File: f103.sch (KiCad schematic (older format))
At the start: 211 parts, among them J1 Conn_01x04_Female, J2 Conn_01x01_Male, J3 Conn_01x01_Male, J4 Conn_01x01_Male, Q1 2N7002, SW1 Rotary_Encoder_Switch, U1 STM32F103CBTx, U2 XC6206P332MR, U3 SRV05-4, Y1 8MHz

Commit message: DRC I
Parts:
- removed J1: Conn_01x04_Female, Connector_PinHeader_2.54mm:PinHeader_1x04_P2.54mm_Vertical, symbol Connector:Conn_01x04_Female
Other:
- note removed: "USB Breakout"
- moved on the sheet: C10, C11, U2, U3
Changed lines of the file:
@@
 EESchema Schematic File Version 4
+LIBS:f103-cache
 EELAYER 30 0
 EELAYER END
@@
 	1    0    0    -1
 $EndComp
-Text GLabel 5800 8050 2    50   Input ~ 0
+Text GLabel 4800 8050 2    50   Input ~ 0
 D-
 $Comp
 L power:+5V #PWR0116
 U 1 1 5FF47CBA
-P 5300 7650
-F 0 "#PWR0116" H 5300 7500 50  0001 C CNN
-F 1 "+5V" H 5315 7823 50  0000 C CNN
-F 2 "" H 5300 7650 50  0001 C CNN
-F 3 "" H 5300 7650 50  0001 C CNN
-	1    5300 7650
+P 4300 7650
+F 0 "#PWR0116" H 4300 7500 50  0001 C CNN
+F 1 "+5V" H 4315 7823 50  0000 C CNN
+F 2 "" H 4300 7650 50  0001 C CNN
+F 3 "" H 4300 7650 50  0001 C CNN
+	1    4300 7650
 	1    0    0    -1
 $EndComp
@@
 L power:GND #PWR0115
 U 1 1 5FF463F5
-P 5300 8650
-F 0 "#PWR0115" H 5300 8400 50  0001 C CNN
-F 1 "GND" H 5305 8477 50  0000 C CNN
-F 2 "" H 5300 8650 50  0001 C CNN
-F 3 "" H 5300 8650 50  0001 C CNN
-	1    5300 8650
+P 4300 8650
+F 0 "#PWR0115" H 4300 8400 50  0001 C CNN
+F 1 "GND" H 4305 8477 50  0000 C CNN
+F 2 "" H 4300 8650 50  0001 C CNN
+F 3 "" H 4300 8650 50  0001 C CNN
+	1    4300 8650
 	1    0    0    -1
 $EndComp
-Text GLabel 5800 8250 2    50   Input ~ 0
+Text GLabel 4800 8250 2    50   Input ~ 0
 D+
 $Comp
 L Power_Protection:SRV05-4 U3
 U 1 1 5FF42D8B
-P 5300 8150
-F 0 "U3" H 5000 8800 50  0000 C CNN
-F 1 "SRV05-4" H 5000 8700 50  0000 C CNN
-F 2 "Package_TO_SOT_SMD:SOT-23-6" H 6000 7700 50  0001 C CNN
-F 3 "http://www.onsemi.com/pub/Collateral/SRV05-4-D.PDF" H 5300 8150 50  0001 C CNN
-F 4 "C85364" H 5300 8150 50  0001 C CNN "Part #"
-	1    5300 8150
+P 4300 8150
+F 0 "U3" H 4000 8800 50  0000 C CNN
+F 1 "SRV05-4" H 4000 8700 50  0000 C CNN
+F 2 "Package_TO_SOT_SMD:SOT-23-6" H 5000 7700 50  0001 C CNN
+F 3 "http://www.onsemi.com/pub/Collateral/SRV05-4-D.PDF" H 4300 8150 50  0001 C CNN
+F 4 "C85364" H 4300 8150 50  0001 C CNN "Part #"
+	1    4300 8150
 	1    0    0    -1
 $EndComp
 Wire Wire Line
-	7450 8550 7000 8550
-Connection ~ 7000 8550
+	6950 8550 6500 8550
+Connection ~ 6500 8550
 Wire Wire Line
-	6550 8550 7000 8550
-Connection ~ 6550 8250
+	6050 8550 6500 8550
+Connection ~ 6050 8250
 Wire Wire Line
-	6550 8250 6450 8250
+	6050 8250 5950 8250
 Wire Wire Line
-	6550 8250 6550 8350
+	6050 8250 6050 8350
 Wire Wire Line
-	6700 8250 6550 8250
-Connection ~ 7450 8250
+	6200 8250 6050 8250
+Connection ~ 6950 8250
 Wire Wire Line
-	7450 8250 7550 8250
+	6950 8250 7050 8250
 Wire Wire Line
-	7450 8250 7450 8350
+	6950 8250 6950 8350
 Wire Wire Line
-	7300 8250 7450 8250
+	6800 8250 6950 8250
 $Comp
 L Device:C_Small C11
 U 1 1 5FF82A05
-P 7450 8450
-F 0 "C11" H 7542 8496 50  0000 L CNN
-F 1 "1uF" H 7542 8405 50  0000 L CNN
-F 2 "Capacitor_SMD:C_0603_1608Metric" H 7450 8450 50  0001 C CNN
-F 3 "~" H 7450 8450 50  0001 C CNN
-	1    7450 8450
+P 6950 8450
+F 0 "C11" H 7042 8496 50  0000 L CNN
+F 1 "1uF" H 7042 8405 50  0000 L CNN
+F 2 "Capacitor_SMD:C_0603_1608Metric" H 6950 8450 50  0001 C CNN
+F 3 "~" H 6950 8450 50  0001 C CNN
+	1    6950 8450
 	1    0    0    -1
 $EndComp
@@
 L Device:C_Small C10
 U 1 1 5FF81242
-P 6550 8450
-F 0 "C10" H 6642 8496 50  0000 L CNN
-F 1 "1uF" H 6642 8405 50  0000 L CNN
-F 2 "Capacitor_SMD:C_0603_1608Metric" H 6550 8450 50  0001 C CNN
-F 3 "~" H 6550 8450 50  0001 C CNN
-	1    6550 8450
+P 6050 8450
+F 0 "C10" H 6142 8496 50  0000 L CNN
+F 1 "1uF" H 6142 8405 50  0000 L CNN
+F 2 "Capacitor_SMD:C_0603_1608Metric" H 6050 8450 50  0001 C CNN
+F 3 "~" H 6050 8450 50  0001 C CNN
+	1    6050 8450
 	1    0    0    -1
 $EndComp
@@
 L power:GND #PWR0119
 U 1 1 5FF7FCD1
-P 7000 8550
-F 0 "#PWR0119" H 7000 8300 50  0001 C CNN
-F 1 "GND" H 7005 8377 50  0000 C CNN
-F 2 "" H 7000 8550 50  0001 C CNN
-F 3 "" H 7000 8550 50  0001 C CNN
-	1    7000 8550
+P 6500 8550
+F 0 "#PWR0119" H 6500 8300 50  0001 C CNN
+F 1 "GND" H 6505 8377 50  0000 C CNN
+F 2 "" H 6500 8550 50  0001 C CNN
+F 3 "" H 6500 8550 50  0001 C CNN
+	1    6500 8550
 	1    0    0    -1
 $EndComp
@@
 L power:+3.3V #PWR0118
 U 1 1 5FF7E7EA
-P 7550 8250
-F 0 "#PWR0118" H 7550 8100 50  0001 C CNN
-F 1 "+3.3V" H 7565 8423 50  0000 C CNN
-F 2 "" H 7550 8250 50  0001 C CNN
-F 3 "" H 7550 8250 50  0001 C CNN
-	1    7550 8250
+P 7050 8250
+F 0 "#PWR0118" H 7050 8100 50  0001 C CNN
+F 1 "+3.3V" H 7065 8423 50  0000 C CNN
+F 2 "" H 7050 8250 50  0001 C CNN
+F 3 "" H 7050 8250 50  0001 C CNN
+	1    7050 8250
 	1    0    0    -1
 $EndComp
@@
 L power:+5V #PWR0117
 U 1 1 5FF7D017
-P 6450 8250
-F 0 "#PWR0117" H 6450 8100 50  0001 C CNN
-F 1 "+5V" H 6465 8423 50  0000 C CNN
-F 2 "" H 6450 8250 50  0001 C CNN
-F 3 "" H 6450 8250 50  0001 C CNN
-	1    6450 8250
+P 5950 8250
+F 0 "#PWR0117" H 5950 8100 50  0001 C CNN
+F 1 "+5V" H 5965 8423 50  0000 C CNN
+F 2 "" H 5950 8250 50  0001 C CNN
+F 3 "" H 5950 8250 50  0001 C CNN
+	1    5950 8250
 	1    0    0    -1
 $EndComp
@@
 L Regulator_Linear:MCP1700-3302E_SOT23 U2
 U 1 1 5FF7B9AE
-P 7000 8250
-F 0 "U2" H 7000 8492 50  0000 C CNN
-F 1 "XC6206P332MR" H 7000 8401 50  0000 C CNN
-F 2 "Package_TO_SOT_SMD:SOT-23" H 7000 8475 50  0001 C CNN
-F 3 "http://ww1.microchip.com/downloads/en/DeviceDoc/20001826D.pdf" H 7000 8250 50  0001 C CNN
-F 4 "C5446" H 7000 8250 50  0001 C CNN "Part #"
-	1    7000 8250
+P 6500 8250
+F 0 "U2" H 6500 8492 50  0000 C CNN
+F 1 "XC6206P332MR" H 6500 8401 50  0000 C CNN
+F 2 "Package_TO_SOT_SMD:SOT-23" H 6500 8475 50  0001 C CNN
+F 3 "http://ww1.microchip.com/downloads/en/DeviceDoc/20001826D.pdf" H 6500 8250 50  0001 C CNN
+F 4 "C5446" H 6500 8250 50  0001 C CNN "Part #"
+	1    6500 8250
 	1    0    0    -1
 $EndComp
@@
 Text Notes 1950 7300 0    98   ~ 20
 USB
-Text Notes 6500 7300 0    98   ~ 20
+Text Notes 6000 7300 0    98   ~ 20
 Voltage Reg.
-Text Notes 5150 7300 0    98   ~ 20
+Text Notes 4150 7300 0    98   ~ 20
 ESD
 NoConn ~ 2050 8400
@@
 	1950 3900 2200 3900
 Connection ~ 2200 3900
-$Comp
-L power:VBUS #PWR0131
-U 1 1 60058240
-P 3500 7900
-F 0 "#PWR0131" H 3500 7750 50  0001 C CNN
-F 1 "VBUS" H 3515 8073 50  0000 C CNN
-F 2 "" H 3500 7900 50  0001 C CNN
-F 3 "" H 3500 7900 50  0001 C CNN
-	1    3500 7900
-	1    0    0    -1
-$EndComp
-$Comp
-L power:GND #PWR0132
-U 1 1 60057E3C
-P 3500 8200
-F 0 "#PWR0132" H 3500 7950 50  0001 C CNN
-F 1 "GND" H 3505 8027 50  0000 C CNN
-F 2 "" H 3500 8200 50  0001 C CNN
-F 3 "" H 3500 8200 50  0001 C CNN
-	1    3500 8200
-	1    0    0    -1
-$EndComp
-Text GLabel 3500 8100 0    50   Input ~ 0
-D+
-Text GLabel 3500 8000 0    50   Input ~ 0
-D-
-$Comp
-L Connector:Conn_01x04_Female J1
-U 1 1 60056004
-P 3700 8000
-F 0 "J1" H 3728 7976 50  0000 L CNN
-F 1 "Conn_01x04_Female" H 3728 7885 50  0000 L CNN
-F 2 "Connector_PinHeader_2.54mm:PinHeader_1x04_P2.54mm_Vertical" H 3700 8000 50  0001 C CNN
-F 3 "~" H 3700 8000 50  0001 C CNN
-	1    3700 8000
-	1    0    0    -1
-$EndComp
 Wire Notes Line
 	550  8900 7800 8900
-Text Notes 3400 7300 0    98   ~ 20
-USB Breakout
 $Comp
 L Device:Rotary_Encoder_Switch SW1

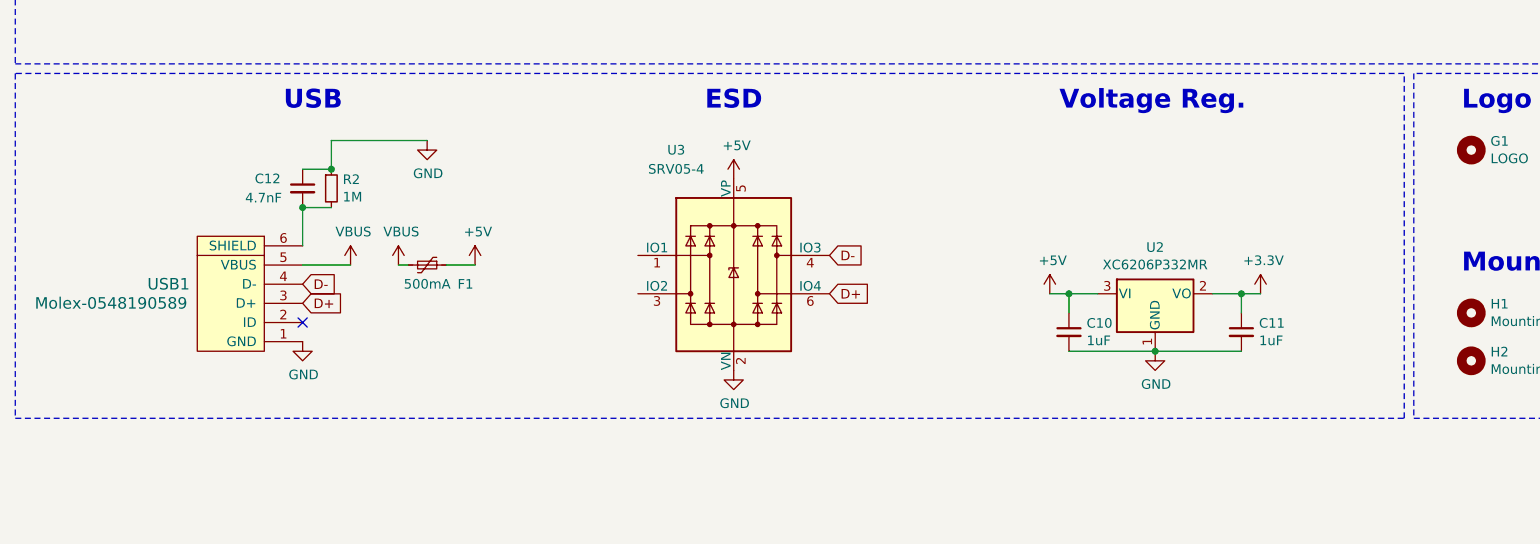
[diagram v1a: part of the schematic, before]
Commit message: DRC III
Switch to usb type-C
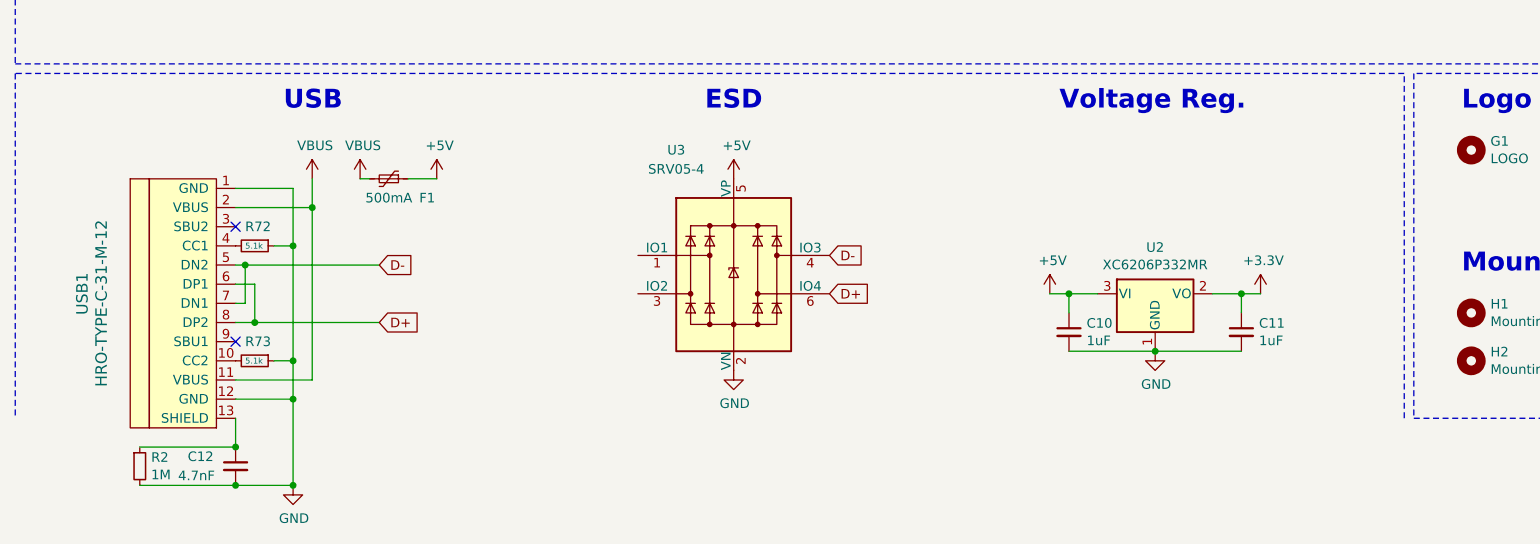
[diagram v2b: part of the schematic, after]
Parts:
- removed USB1: Molex-0548190589, MINI:Molex-0548190589, symbol RKP:Molex-0548190589
- added R72, R73: 5.1k, Resistor_SMD:R_0603_1608Metric, symbol Device:R_Small
- added USB1: HRO-TYPE-C-31-M-12, Type C:HRO-TYPE-C-31-M-12-jlc, symbol Type-C:HRO-TYPE-C-31-M-12
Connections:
- net D+: now also USB1.6 (DP1), USB1.8 (DP2)
- net D-: now also USB1.5 (DN2), USB1.7 (DN1)
- net GND: now also C12.2, R2.2, R72.1, R73.1, USB1.1 (GND), USB1.12 (GND); no longer C12.1, R2.1
- net VBUS: now also USB1.11 (VBUS), USB1.2 (VBUS)
- new net: C12.1, R2.1, USB1.13 (SHIELD)
- new net: R73.2, USB1.10 (CC2)
- new net: R72.2, USB1.4 (CC1)
- no-connect marks 9 -> 10
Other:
- moved on the sheet: C12, F1, R2
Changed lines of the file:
@@
 $EndComp
 Wire Wire Line
-	2950 8100 2800 8100
-$Comp
-L RKP:Molex-0548190589 USB1
-U 1 1 5FEC9337
-P 1750 8300
-F 0 "USB1" V 1850 8700 60  0000 C CNN
-F 1 "Molex-0548190589" V 1750 9000 60  0000 C CNN
-F 2 "MINI:Molex-0548190589" H 1750 8300 60  0001 C CNN
-F 3 "" H 1750 8300 60  0001 C CNN
-	1    1750 8300
-	0    -1   -1   0
-$EndComp
+	2750 7650 2600 7650
 $Comp
 L Device:R_Small R1
@@
 $EndComp
 $Comp
-L power:GND #PWR0125
-U 1 1 600ED86F
-P 2700 7450
-F 0 "#PWR0125" H 2700 7200 50  0001 C CNN
-F 1 "GND" H 2705 7277 50  0000 C CNN
-F 2 "" H 2700 7450 50  0001 C CNN
-F 3 "" H 2700 7450 50  0001 C CNN
-	1    2700 7450
-	1    0    0    -1
-$EndComp
-$Comp
 L Device:R_Small R2
 U 1 1 600E6AC0
-P 2200 7700
-F 0 "R2" H 2259 7746 50  0000 L CNN
-F 1 "1M" H 2259 7655 50  0000 L CNN
-F 2 "Resistor_SMD:R_0603_1608Metric" H 2200 7700 50  0001 C CNN
-F 3 "~" H 2200 7700 50  0001 C CNN
-	1    2200 7700
+P 1200 9150
+F 0 "R2" H 1259 9196 50  0000 L CNN
+F 1 "1M" H 1259 9105 50  0000 L CNN
+F 2 "Resistor_SMD:R_0603_1608Metric" H 1200 9150 50  0001 C CNN
+F 3 "~" H 1200 9150 50  0001 C CNN
+	1    1200 9150
 	1    0    0    -1
 $EndComp
@@
 L Device:C_Small C12
 U 1 1 600E54EB
-P 2050 7700
-F 0 "C12" H 1800 7750 50  0000 L CNN
-F 1 "4.7nF" H 1750 7650 50  0000 L CNN
-F 2 "Capacitor_SMD:C_0603_1608Metric" H 2050 7700 50  0001 C CNN
-F 3 "~" H 2050 7700 50  0001 C CNN
-	1    2050 7700
+P 1700 9150
+F 0 "C12" H 1450 9200 50  0000 L CNN
+F 1 "4.7nF" H 1400 9100 50  0000 L CNN
+F 2 "Capacitor_SMD:C_0603_1608Metric" H 1700 9150 50  0001 C CNN
+F 3 "~" H 1700 9150 50  0001 C CNN
+	1    1700 9150
 	1    0    0    -1
 $EndComp
@@
 L power:+5V #PWR0123
 U 1 1 5FFD8345
-P 2950 8100
-F 0 "#PWR0123" H 2950 7950 50  0001 C CNN
-F 1 "+5V" H 2965 8273 50  0000 C CNN
-F 2 "" H 2950 8100 50  0001 C CNN
-F 3 "" H 2950 8100 50  0001 C CNN
-	1    2950 8100
+P 2750 7650
+F 0 "#PWR0123" H 2750 7500 50  0001 C CNN
+F 1 "+5V" H 2765 7823 50  0000 C CNN
+F 2 "" H 2750 7650 50  0001 C CNN
+F 3 "" H 2750 7650 50  0001 C CNN
+	1    2750 7650
 	1    0    0    -1
 $EndComp
@@
 L Device:Polyfuse_Small F1
 U 1 1 5FFD669E
-P 2700 8100
-F 0 "F1" V 2800 8300 50  0000 C CNN
-F 1 "500mA" V 2800 8100 50  0000 C CNN
-F 2 "Fuse:Fuse_1206_3216Metric" H 2750 7900 50  0001 L CNN
-F 3 "~" H 2700 8100 50  0001 C CNN
-F 4 "C369159" V 2700 8100 50  0001 C CNN "Part #"
-	1    2700 8100
+P 2500 7650
+F 0 "F1" V 2600 7850 50  0000 C CNN
+F 1 "500mA" V 2600 7650 50  0000 C CNN
+F 2 "Fuse:Fuse_1206_3216Metric" H 2550 7450 50  0001 L CNN
+F 3 "~" H 2500 7650 50  0001 C CNN
+F 4 "C369159" V 2500 7650 50  0001 C CNN "Part #"
+	1    2500 7650
 	0    1    1    0
 $EndComp
@@
 L power:GND #PWR0120
 U 1 1 5FFD3143
-P 2050 8500
-F 0 "#PWR0120" H 2050 8250 50  0001 C CNN
-F 1 "GND" H 2055 8327 50  0000 C CNN
-F 2 "" H 2050 8500 50  0001 C CNN
-F 3 "" H 2050 8500 50  0001 C CNN
-	1    2050 8500
-	1    0    0    -1
-$EndComp
-Text GLabel 2050 8300 2    50   Input ~ 0
-D+
-Text GLabel 2050 8200 2    50   Input ~ 0
-D-
+P 2000 9250
+F 0 "#PWR0120" H 2000 9000 50  0001 C CNN
+F 1 "GND" H 2005 9077 50  0000 C CNN
+F 2 "" H 2000 9250 50  0001 C CNN
+F 3 "" H 2000 9250 50  0001 C CNN
+	1    2000 9250
+	1    0    0    -1
+$EndComp
 Text GLabel 13500 6500 2    50   Input ~ 0
 BOOT0
@@
 $EndComp
 Wire Wire Line
-	2300 8100 2050 8100
-Wire Wire Line
-	2550 8100 2600 8100
-Wire Wire Line
-	2050 8000 2050 7800
-Wire Wire Line
-	2050 7800 2200 7800
-Connection ~ 2050 7800
-Wire Wire Line
-	2050 7600 2200 7600
-Wire Wire Line
-	2200 7600 2200 7450
-Wire Wire Line
-	2200 7450 2700 7450
-Connection ~ 2200 7600
-$Comp
-L power:VBUS #PWR0129
-U 1 1 6015B2FA
-P 2300 8100
-F 0 "#PWR0129" H 2300 7950 50  0001 C CNN
-F 1 "VBUS" H 2315 8273 50  0000 C CNN
-F 2 "" H 2300 8100 50  0001 C CNN
-F 3 "" H 2300 8100 50  0001 C CNN
-	1    2300 8100
-	1    0    0    -1
-$EndComp
+	2350 7650 2400 7650
 $Comp
 L power:VBUS #PWR0130
 U 1 1 6015CEDE
-P 2550 8100
-F 0 "#PWR0130" H 2550 7950 50  0001 C CNN
-F 1 "VBUS" H 2565 8273 50  0000 C CNN
-F 2 "" H 2550 8100 50  0001 C CNN
-F 3 "" H 2550 8100 50  0001 C CNN
-	1    2550 8100
+P 2350 7650
+F 0 "#PWR0130" H 2350 7500 50  0001 C CNN
+F 1 "VBUS" H 2365 7823 50  0000 C CNN
+F 2 "" H 2350 7650 50  0001 C CNN
+F 3 "" H 2350 7650 50  0001 C CNN
+	1    2350 7650
 	1    0    0    -1
 $EndComp
@@
 Text Notes 4150 7300 0    98   ~ 20
 ESD
-NoConn ~ 2050 8400
 NoConn ~ 14000 3400
 NoConn ~ 14000 3500
@@
 	1950 3900 2200 3900
 Connection ~ 2200 3900
-Wire Notes Line
-	550  8900 7800 8900
 $Comp
 L Device:Rotary_Encoder_Switch SW1
@@
 	10700 1800 10700 2700
 Connection ~ 10600 1900
+$Comp
+L Type-C:HRO-TYPE-C-31-M-12 USB1
+U 1 1 601D2A97
+P 1600 8250
+F 0 "USB1" V 900 8250 60  0000 C CNN
+F 1 "HRO-TYPE-C-31-M-12" V 1000 8200 60  0000 C CNN
+F 2 "Type C:HRO-TYPE-C-31-M-12-jlc" H 1600 8250 60  0001 C CNN
+F 3 "" H 1600 8250 60  0001 C CNN
+	1    1600 8250
+	1    0    0    -1
+$EndComp
+Wire Wire Line
+	1200 9050 1700 9050
+Wire Wire Line
+	1700 9050 1700 8900
+Connection ~ 1700 9050
+Wire Wire Line
+	1200 9250 1700 9250
+$Comp
+L Device:R_Small R73
+U 1 1 6023F787
+P 1800 8600
+F 0 "R73" V 1700 8550 50  0000 L CNN
+F 1 "5.1k" V 1800 8550 31  0000 L CNN
+F 2 "Resistor_SMD:R_0603_1608Metric" H 1800 8600 50  0001 C CNN
+F 3 "~" H 1800 8600 50  0001 C CNN
+	1    1800 8600
+	0    1    1    0
+$EndComp
+$Comp
+L Device:R_Small R72
+U 1 1 60241B9D
+P 1800 8000
+F 0 "R72" V 1700 7950 50  0000 L CNN
+F 1 "5.1k" V 1800 7950 31  0000 L CNN
+F 2 "Resistor_SMD:R_0603_1608Metric" H 1800 8000 50  0001 C CNN
+F 3 "~" H 1800 8000 50  0001 C CNN
+	1    1800 8000
+	0    1    1    0
+$EndComp
+Wire Wire Line
+	1700 7700 2000 7700
+Wire Wire Line
+	2000 7700 2000 8000
+Wire Wire Line
+	2000 8800 1700 8800
+Wire Wire Line
+	1900 8600 2000 8600
+Connection ~ 2000 8600
+Wire Wire Line
+	2000 8600 2000 8800
+Wire Wire Line
+	1900 8000 2000 8000
+Connection ~ 2000 8000
+Wire Wire Line
+	2000 8000 2000 8600
+Wire Wire Line
+	1700 8100 1750 8100
+Wire Wire Line
+	1750 8100 1750 8300
+Wire Wire Line
+	1750 8300 1700 8300
+Wire Wire Line
+	1750 8100 2450 8100
+Connection ~ 1750 8100
+Text GLabel 2450 8100 2    50   Input ~ 0
+D-
+Wire Wire Line
+	1700 8200 1800 8200
+Wire Wire Line
+	1800 8200 1800 8400
+Wire Wire Line
+	1800 8400 1700 8400
+Wire Wire Line
+	1800 8400 2450 8400
+Connection ~ 1800 8400
+Text GLabel 2450 8400 2    50   Input ~ 0
+D+
+Wire Wire Line
+	1700 7800 2100 7800
+Wire Wire Line
+	2100 7800 2100 8700
+Wire Wire Line
+	2100 8700 1700 8700
+$Comp
+L power:VBUS #PWR0125
+U 1 1 603FD33D
+P 2100 7650
+F 0 "#PWR0125" H 2100 7500 50  0001 C CNN
+F 1 "VBUS" H 2115 7823 50  0000 C CNN
+F 2 "" H 2100 7650 50  0001 C CNN
+F 3 "" H 2100 7650 50  0001 C CNN
+	1    2100 7650
+	1    0    0    -1
+$EndComp
+Wire Wire Line
+	2100 7650 2100 7800
+Connection ~ 2100 7800
+NoConn ~ 1700 7900
+NoConn ~ 1700 8500
+Wire Wire Line
+	2000 8800 2000 9250
+Wire Wire Line
+	2000 9250 1700 9250
+Connection ~ 2000 8800
+Connection ~ 1700 9250
+Connection ~ 2000 9250
 $EndSCHEMATC

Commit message: DRC IV
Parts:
- USB1: footprint Type C:HRO-TYPE-C-31-M-12-jlc -> edits:HRO-TYPE-C-31-M-12-jlc
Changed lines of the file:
@@
 F 0 "USB1" V 900 8250 60  0000 C CNN
 F 1 "HRO-TYPE-C-31-M-12" V 1000 8200 60  0000 C CNN
-F 2 "Type C:HRO-TYPE-C-31-M-12-jlc" H 1600 8250 60  0001 C CNN
+F 2 "edits:HRO-TYPE-C-31-M-12-jlc" H 1600 8250 60  0001 C CNN
 F 3 "" H 1600 8250 60  0001 C CNN
 	1    1600 8250

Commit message: Checking Datasheet
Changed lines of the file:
@@
 L power:GND #PWR0133
 U 1 1 600CA7BC
-P 950 2100
-F 0 "#PWR0133" H 950 1850 50  0001 C CNN
-F 1 "GND" H 955 1927 50  0000 C CNN
-F 2 "" H 950 2100 50  0001 C CNN
-F 3 "" H 950 2100 50  0001 C CNN
-	1    950  2100
+P 950 2350
+F 0 "#PWR0133" H 950 2100 50  0001 C CNN
+F 1 "GND" H 955 2177 50  0000 C CNN
+F 2 "" H 950 2350 50  0001 C CNN
+F 3 "" H 950 2350 50  0001 C CNN
+	1    950  2350
 	1    0    0    -1
 $EndComp
@@
 Connection ~ 1700 9250
 Connection ~ 2000 9250
+Wire Wire Line
+	950  2350 950  2100
 $EndSCHEMATC

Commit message: DRC Pass
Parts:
- removed J2, J3, J4: Conn_01x01_Male, TestPoint:TestPoint_Pad_D1.5mm, symbol Connector:Conn_01x01_Male
- added J1, J2, J3, J4: Conn_01x01_Female, TestPoint:TestPoint_Pad_D1.5mm, symbol Connector:Conn_01x01_Female
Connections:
- net +3V3: now also J4.1 (Pin_1)
- net C0: now also U1.20 (PB2); no longer U1.19 (PB1)
- net C1: now also U1.19 (PB1); no longer U1.18 (PB0)
- net C14: now also U1.3 (PC14); no longer U1.11 (PA1)
- net C2: now also U1.18 (PB0); no longer U1.17 (PA7)
- net C3: now also U1.17 (PA7); no longer U1.16 (PA6)
- net C4: now also U1.16 (PA6); no longer U1.15 (PA5)
- net C5: now also U1.15 (PA5); no longer U1.14 (PA4)
- net C6: now also U1.14 (PA4); no longer U1.13 (PA3)
- net C7: now also U1.22 (PB11); no longer U1.12 (PA2)
- net ENCA: now also U1.29 (PA8); no longer U1.30 (PA9)
- net ENCB: now also U1.30 (PA9); no longer U1.31 (PA10)
- net GND: now also J2.1 (Pin_1)
- net R0: now also U1.31 (PA10); no longer U1.29 (PA8)
- net R1: now also U1.21 (PB10); no longer U1.20 (PB2)
- net R3: now also U1.13 (PA3); no longer U1.21 (PB10)
- net R4: now also U1.12 (PA2); no longer U1.22 (PB11)
- net SWCLK: now also J3.1 (Pin_1)
- net SWDIO: now also J1.1 (Pin_1)
- no-connect marks 10 -> 9
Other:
- moved on the sheet: C10, C11, C12, D3, F1, R2, R72, R73, U2, USB1
